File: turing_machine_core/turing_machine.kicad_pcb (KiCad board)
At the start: 2 copper layers, 165.1 x 110.5 mm, 58 parts, among them J1 External Interface, J2 Symbol Register Value Output, J3 State Register Value Output, J4 Header Position Value Output, U1 74LS04, U10 AS6C1008, U11 74LS193, U12 74LS374, U13 74LS74, U14 74LS245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

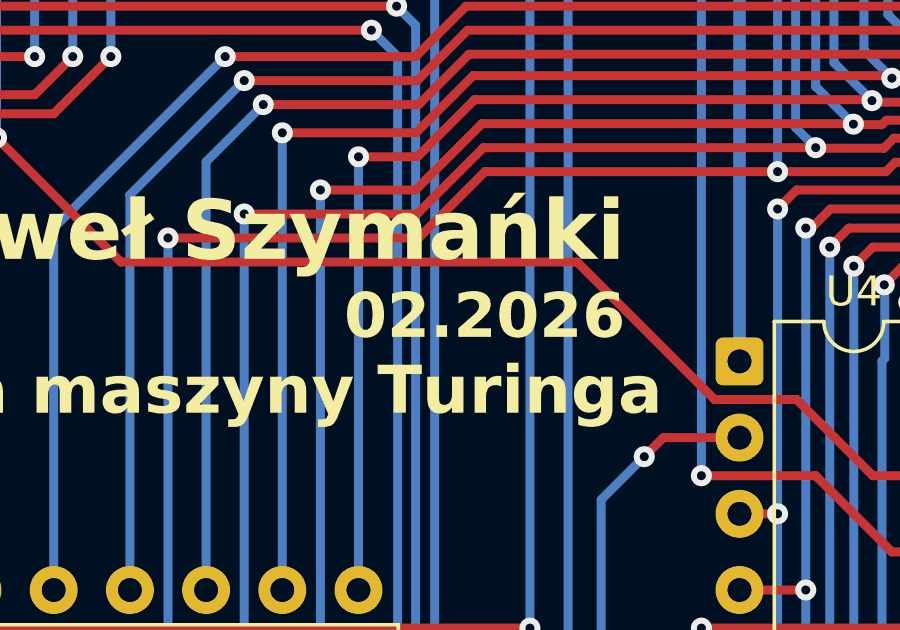
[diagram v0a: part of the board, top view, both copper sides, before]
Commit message: added few markings to PCBs
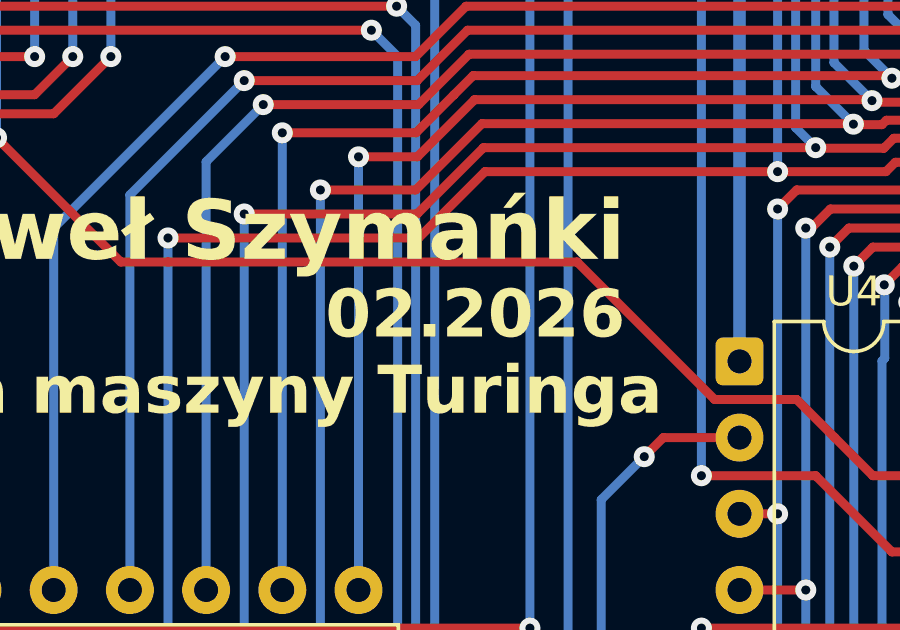
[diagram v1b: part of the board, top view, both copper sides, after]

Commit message: added github links to core and driver boards
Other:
- board text added: "https://github.com/szymanp135/Tura"
- board text removed: "Paweł Szymański 02.2026"
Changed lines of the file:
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@@
-	)
-	(gr_rect
-		(start 162.179 121.285)
-		(end 167.259 126.365)
-		(stroke
-			(width 0.3)
-			(type solid)
-		)
-		(fill yes)
-		(layer "B.Cu")
-		(net 1)
 	)
 	(gr_rect
@@
 	(gr_rect
 		(start 33.02 121.285)
-		(end 113.157 126.365)
-		(stroke
-			(width 0.3)
-			(type solid)
-		)
-		(fill yes)
-		(layer "B.Cu")
-		(net 1)
-	)
-	(gr_rect
-		(start 177.165 121.285)
-		(end 182.88 126.365)
-		(stroke
-			(width 0.3)
-			(type solid)
-		)
-		(fill yes)
-		(layer "B.Cu")
-		(net 1)
-	)
-	(gr_rect
-		(start 113.03 125.984)
-		(end 162.56 126.365)
-		(stroke
-			(width 0.3)
-			(type solid)
-		)
-		(fill yes)
-		(layer "B.Cu")
-		(net 1)
-	)
-	(gr_rect
-		(start 165.989 125.095)
-		(end 177.038 126.365)
+		(end 183.007 126.365)
 		(stroke
 			(width 0.3)
@@
 		(net 1)
 	)
-	(gr_rect
-		(start 113.03 121.285)
-		(end 162.56 121.92)
-		(stroke
-			(width 0.3)
-			(type solid)
-		)
-		(fill yes)
-		(layer "B.Cu")
-		(net 1)
-	)
 	(gr_circle
 		(center 186.69 123.19)
@@
 		(layer "Edge.Cuts")
 	)
-	(gr_text "Tura"
-		(locked yes)
-		(at 177.165 125.095 0)
-		(layer "B.Cu" knockout)
+	(gr_text "C"
+		(at 26.67 40.005 0)
+		(layer "F.SilkS")
 		(effects
 			(font
@@
 				(bold yes)
 			)
-			(justify left bottom mirror)
-		)
-	)
-	(gr_text "Paweł Szymański   02.2026"
-		(at 162.56 125.095 0)
-		(layer "B.Cu" knockout)
-		(effects
-			(font
-				(size 2.3 2.3)
-				(thickness 0.46)
-				(bold yes)
-			)
-			(justify left bottom mirror)
-		)
-	)
-	(gr_text "C"
-		(at 26.67 40.005 0)
+			(justify left bottom)
+		)
+	)
+	(gr_text "(SYMBOL TRANSLATOR)"
+		(at 77.47 120.015 0)
+		(layer "F.SilkS")
+		(effects
+			(font
+				(size 1 1)
+				(thickness 0.15)
+			)
+			(justify left bottom)
+		)
+	)
+	(gr_text "8"
+		(at 160.02 125.73 0)
+		(layer "F.SilkS")
+		(effects
+			(font
+				(size 2 2)
+				(thickness 0.4)
+				(bold yes)
+			)
+			(justify left bottom)
+		)
+	)
+	(gr_text "(TAPE)"
+		(at 147.955 89.535 0)
+		(layer "F.SilkS")
+		(effects
+			(font
+				(size 1 1)
+				(thickness 0.15)
+			)
+			(justify left bottom)
+		)
+	)
+	(gr_text "A"
+		(at 26.035 111.125 0)
 		(layer "F.SilkS")
 		(effects
@@
 		)
 	)
-	(gr_text "(SYMBOL TRANSLATOR)"
-		(at 77.47 120.015 0)
+	(gr_text "B"
+		(at 26.67 75.565 0)
+		(layer "F.SilkS")
+		(effects
+			(font
+				(size 3 3)
+				(thickness 0.6)
+				(bold yes)
+			)
+			(justify left bottom)
+		)
+	)
+	(gr_text "02.2026"
+		(at 82.55 62.865 0)
+		(layer "F.SilkS")
+		(effects
+			(font
+				(size 1.6 1.6)
+				(thickness 0.32)
+				(bold yes)
+			)
+			(justify right bottom)
+		)
+	)
+	(gr_text "4"
+		(at 88.9 125.73 0)
+		(layer "F.SilkS")
+		(effects
+			(font
+				(size 2 2)
+				(thickness 0.4)
+				(bold yes)
+			)
+			(justify left bottom)
+		)
+	)
+	(gr_text "5"
+		(at 106.68 125.73 0)
+		(layer "F.SilkS")
+		(effects
+			(font
+				(size 2 2)
+				(thickness 0.4)
+				(bold yes)
+			)
+			(justify left bottom)
+		)
+	)
+	(gr_text "7"
+		(at 142.24 125.73 0)
+		(layer "F.SilkS")
+		(effects
+			(font
+				(size 2 2)
+				(thickness 0.4)
+				(bold yes)
+			)
+			(justify left bottom)
+		)
+	)
+	(gr_text "9\n"
+		(at 177.8 125.73 0)
+		(layer "F.SilkS")
+		(effects
+			(font
+				(size 2 2)
+				(thickness 0.4)
+				(bold yes)
+			)
+			(justify left bottom)
+		)
+	)
+	(gr_text "2"
+		(at 53.34 125.73 0)
+		(layer "F.SilkS")
+		(effects
+			(font
+				(size 2 2)
+				(thickness 0.4)
+				(bold yes)
+			)
+			(justify left bottom)
+		)
+	)
+	(gr_text "(STATE TRANSLATOR)"
+		(at 59.69 89.535 0)
 		(layer "F.SilkS")
 		(effects
@@
 		)
 	)
-	(gr_text "8"
-		(at 160.02 125.73 0)
-		(layer "F.SilkS")
-		(effects
-			(font
-				(size 2 2)
-				(thickness 0.4)
-				(bold yes)
-			)
-			(justify left bottom)
-		)
-	)
-	(gr_text "(TAPE)"
-		(at 147.955 89.535 0)
-		(layer "F.SilkS")
-		(effects
-			(font
-				(size 1 1)
-				(thickness 0.15)
-			)
-			(justify left bottom)
-		)
-	)
-	(gr_text "A"
-		(at 26.035 111.125 0)
-		(layer "F.SilkS")
-		(effects
-			(font
-				(size 3 3)
-				(thickness 0.6)
-				(bold yes)
-			)
-			(justify left bottom)
-		)
-	)
-	(gr_text "B"
-		(at 26.67 75.565 0)
-		(layer "F.SilkS")
-		(effects
-			(font
-				(size 3 3)
-				(thickness 0.6)
-				(bold yes)
-			)
-			(justify left bottom)
-		)
-	)
-	(gr_text "02.2026"
-		(at 82.55 62.865 0)
+	(gr_text "Fizyczna implementacja maszyny Turinga"
+		(at 32.385 65.405 0)
 		(layer "F.SilkS")
 		(effects
@@
 				(bold yes)
 			)
-			(justify right bottom)
-		)
-	)
-	(gr_text "4"
-		(at 88.9 125.73 0)
-		(layer "F.SilkS")
-		(effects
-			(font
-				(size 2 2)
-				(thickness 0.4)
-				(bold yes)
-			)
-			(justify left bottom)
-		)
-	)
-	(gr_text "5"
-		(at 106.68 125.73 0)
-		(layer "F.SilkS")
-		(effects
-			(font
-				(size 2 2)
-				(thickness 0.4)
-				(bold yes)
-			)
-			(justify left bottom)
-		)
-	)
-	(gr_text "7"
-		(at 142.24 125.73 0)
-		(layer "F.SilkS")
-		(effects
-			(font
-				(size 2 2)
-				(thickness 0.4)
-				(bold yes)
-			)
-			(justify left bottom)
-		)
-	)
-	(gr_text "9\n"
-		(at 177.8 125.73 0)
-		(layer "F.SilkS")
-		(effects
-			(font
-				(size 2 2)
-				(thickness 0.4)
-				(bold yes)
-			)
-			(justify left bottom)
-		)
-	)
-	(gr_text "2"
-		(at 53.34 125.73 0)
-		(layer "F.SilkS")
-		(effects
-			(font
-				(size 2 2)
-				(thickness 0.4)
-				(bold yes)
-			)
-			(justify left bottom)
-		)
-	)
-	(gr_text "(STATE TRANSLATOR)"
-		(at 59.69 89.535 0)
-		(layer "F.SilkS")
-		(effects
-			(font
-				(size 1 1)
-				(thickness 0.15)
-			)
-			(justify left bottom)
-		)
-	)
-	(gr_text "Fizyczna implementacja maszyny Turinga"
-		(at 32.385 65.405 0)
-		(layer "F.SilkS")
-		(effects
-			(font
-				(size 1.6 1.6)
-				(thickness 0.32)
-				(bold yes)
-			)
 			(justify left bottom)
 		)
@@
 		)
 	)
+	(gr_text "https://github.com/szymanp135/Tura"
+		(at 180.975 125.095 0)
+		(layer "B.SilkS")
+		(effects
+			(font
+				(size 2 2)
+				(thickness 0.25)
+			)
+			(justify left bottom mirror)
+		)
+	)
